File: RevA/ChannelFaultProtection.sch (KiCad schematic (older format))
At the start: 1 part

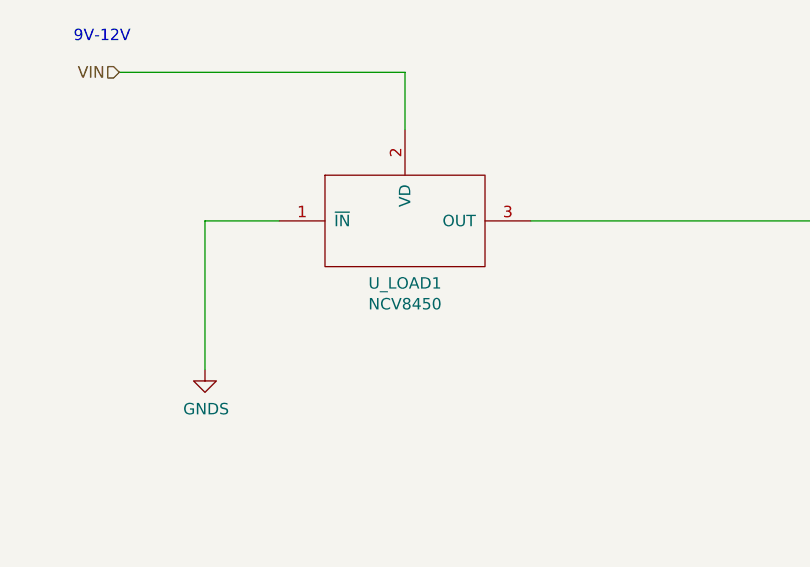
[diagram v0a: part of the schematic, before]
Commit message: updated HW
changed single gang PTD901 to dual gang concentric PTH901
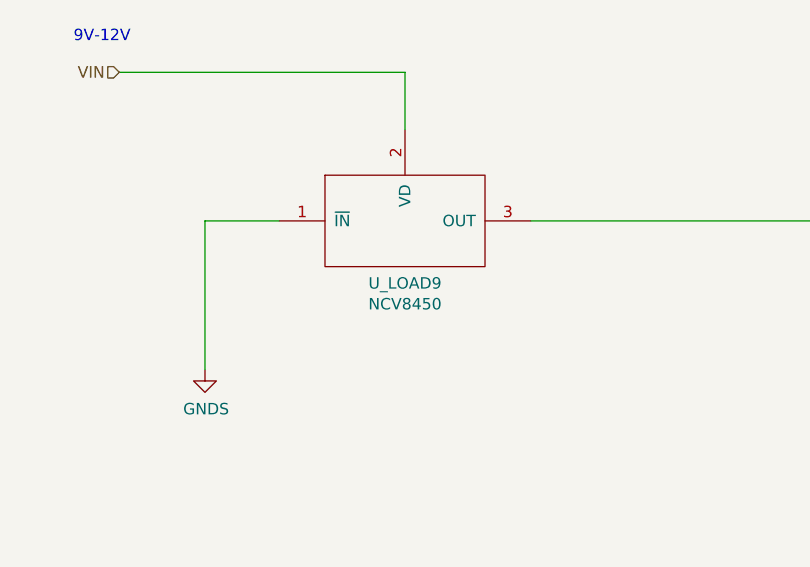
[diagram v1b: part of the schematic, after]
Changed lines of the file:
@@
 AR Path="/5DF46F3E/5DF57DA8" Ref="U_LOAD8"  Part="1"
 AR Path="/5DF61078/5DF57DA8" Ref="U_LOAD9"  Part="1"
-F 0 "U_LOAD1" H 5950 2677 50  0000 C CNN
+F 0 "U_LOAD9" H 5950 2677 50  0000 C CNN
 F 1 "NCV8450" H 5950 2586 50  0000 C CNN
 F 2 "Package_TO_SOT_SMD:SOT-223-3_TabPin2" H 5950 2700 50  0001 C CNN
@@
 AR Path="/5DF46F3E/5DF5C5FE" Ref="#PWR045"  Part="1"
 AR Path="/5DF61078/5DF5C5FE" Ref="#PWR047"  Part="1"
-F 0 "#PWR038" H 5075 3350 50  0001 C CNN
+F 0 "#PWR047" H 5075 3350 50  0001 C CNN
 F 1 "GNDS" H 5080 3427 50  0000 C CNN
 F 2 "" H 5075 3600 50  0001 C CNN
